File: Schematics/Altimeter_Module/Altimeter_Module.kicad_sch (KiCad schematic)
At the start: 102 parts, among them J1 Stack Male Edge Connector, J2 Main E-Match, J3 Drogue E-Match, J4 USB_B_Micro, J5 SWD_01x04_Pin, Q1 AO3400A, Q2 AO4406AL, Q3 AO3400A, Q4 AO3400A, Q5 AO4406AL, SW1 SW_STM_RESET, SW2 SW_STM_BOOT_MODE, U1 KX134-1211, U10 ACS70331EOLC, U12 AMS1117-3.3, U2 MS560702BA03-50, U3 W25Q128JVS, U4 LM66100DCKR, U5 LM66100DCKR, U6 STM32F103CBTx, U7 LM66100DCKR, U8 ISO1042BDWVR, U9 MPU-6050, Y1 X322516MMB4SI

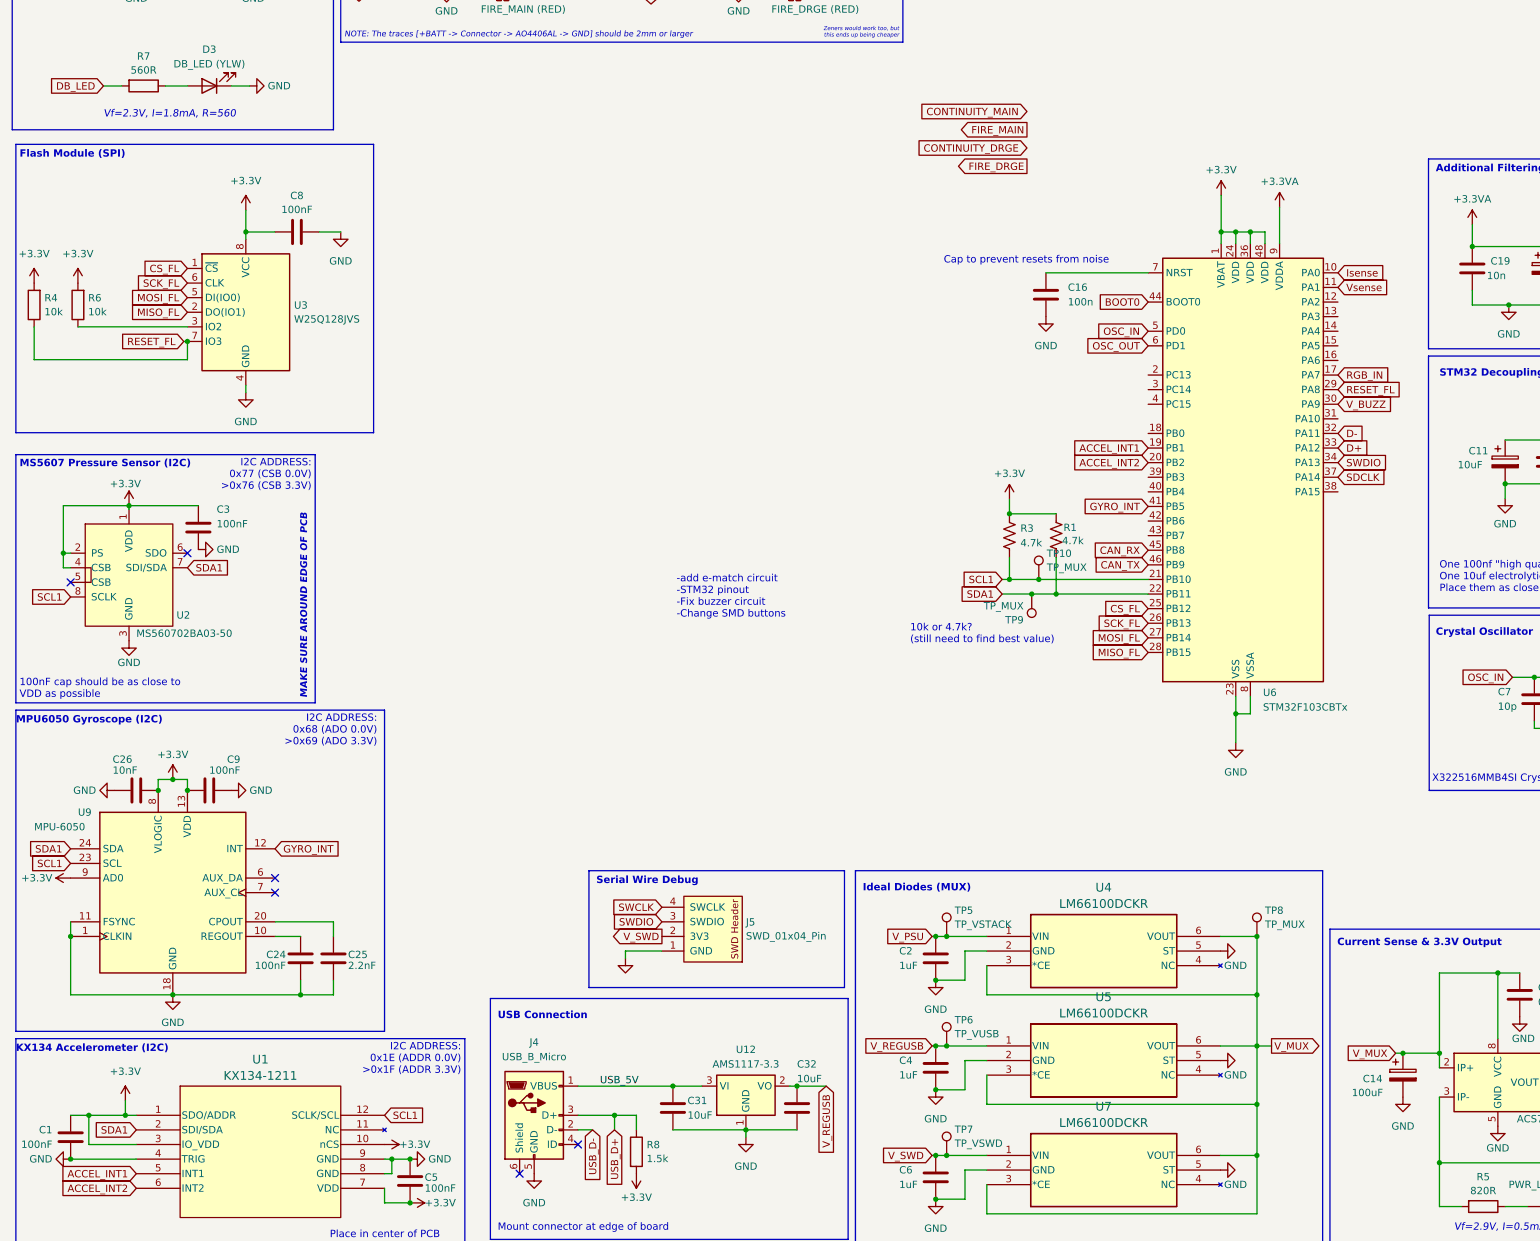
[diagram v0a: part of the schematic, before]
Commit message: Updated STM32 pinout
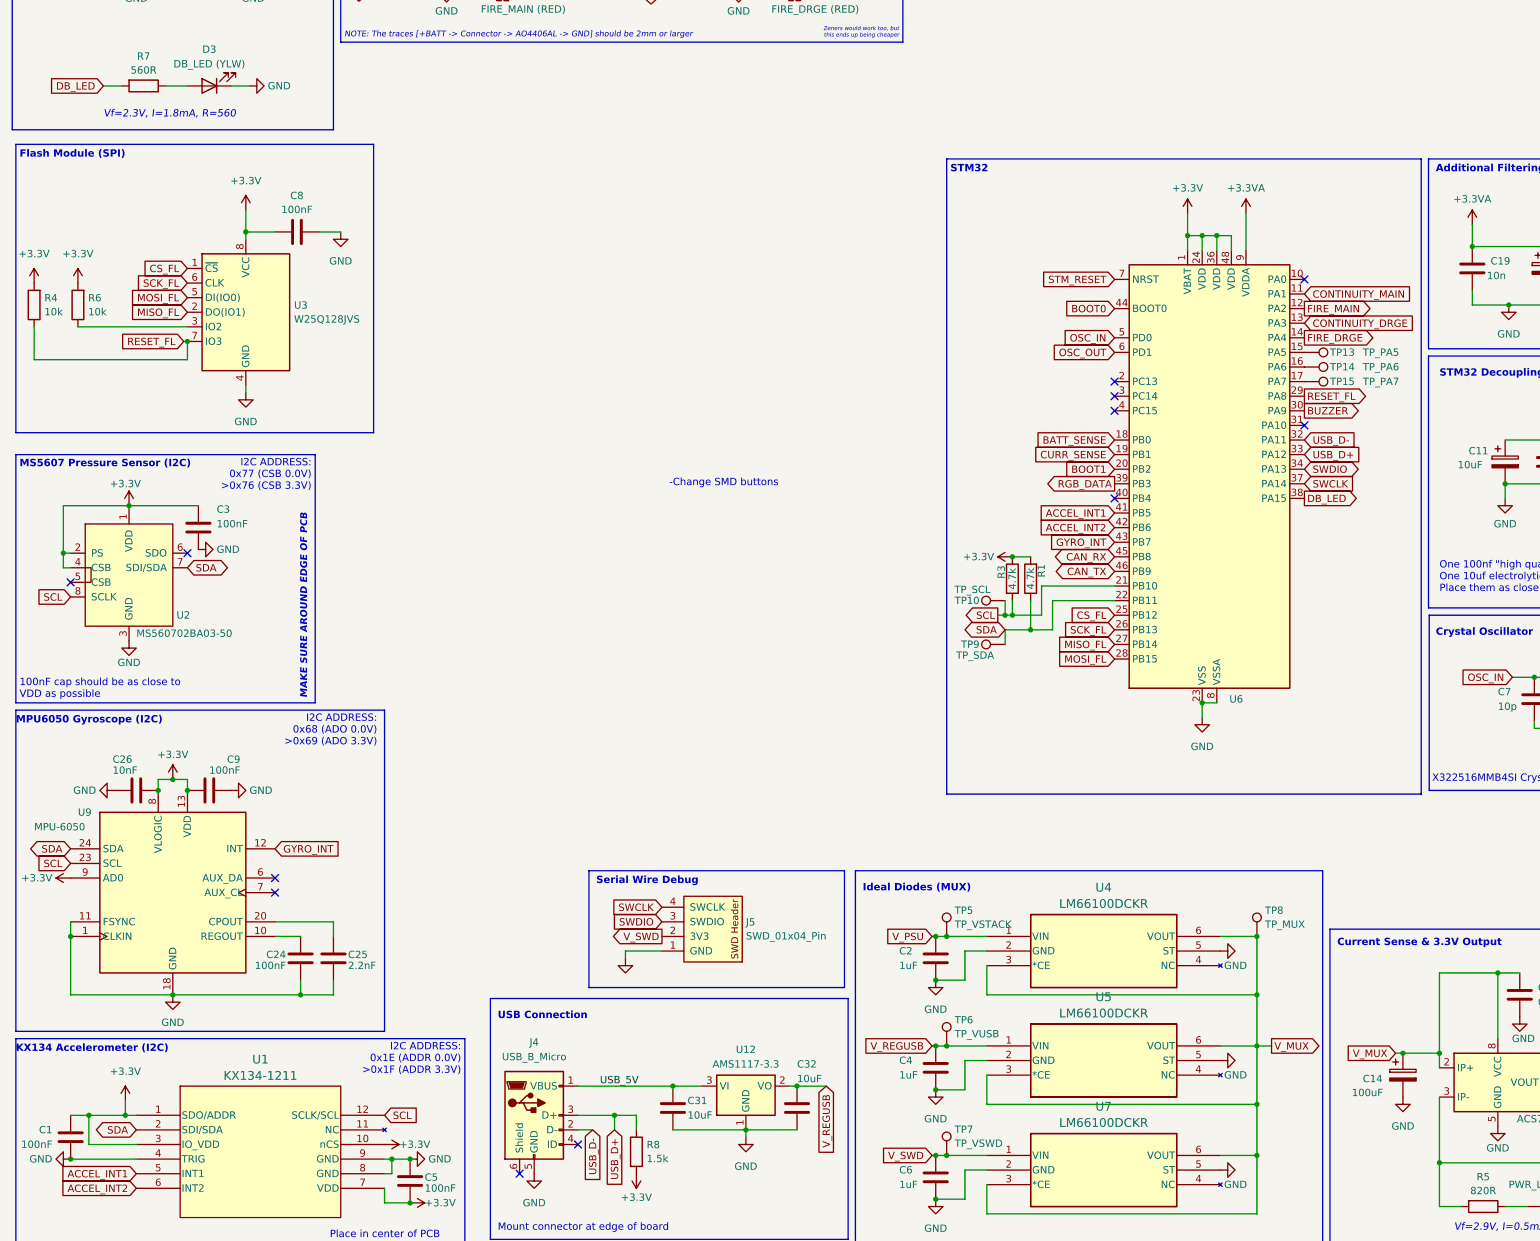
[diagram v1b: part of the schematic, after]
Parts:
- removed C16: 100n, symbol Device:C
- removed R1, R3: 4.7k, symbol Device:R_US
- added R1, R3: 4.7k, Resistor_SMD:R_0603_1608Metric, symbol Device:R
- added TP13: TP_PA5, TestPoint:TestPoint_Pad_1.5x1.5mm, symbol Connector:TestPoint
- added TP14: TP_PA6, TestPoint:TestPoint_Pad_1.5x1.5mm, symbol Connector:TestPoint
- added TP15: TP_PA7, TestPoint:TestPoint_Pad_1.5x1.5mm, symbol Connector:TestPoint
- TP10: value TP_MUX -> TP_SCL
- TP9: value TP_MUX -> TP_SDA
- U6: LCSC (none) -> C8304
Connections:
- net D+ is gone; now on net USB_D+: U6.33 (PA12)
- net D- is gone; now on net USB_D-: U6.32 (PA11)
- net SDCLK is gone; now on net SWCLK: U6.37 (PA14)
- net V_BUZZ is gone; now on net BUZZER: U6.30 (PA9)
- net Vsense is gone; now on net CONTINUITY_MAIN: U6.11 (PA1)
- net +3.3V: now also R1.2, R3.1
- net ACCEL_INT1: now also U6.41 (PB5); no longer U6.19 (PB1)
- net ACCEL_INT2: now also U6.42 (PB6); no longer U6.20 (PB2)
- net BATT_SENSE: now also U6.18 (PB0)
- net BOOT1: now also U6.20 (PB2)
- net CONTINUITY_DRGE: now also U6.13 (PA3)
- net CURR_SENSE: now also U6.19 (PB1)
- net DB_LED: now also U6.38 (PA15)
- net FIRE_DRGE: now also U6.14 (PA4)
- net FIRE_MAIN: now also U6.12 (PA2)
- net GYRO_INT: now also U6.43 (PB7); no longer U6.41 (PB5)
- net MISO_FL: now also U6.27 (PB14); no longer U6.28 (PB15)
- net MOSI_FL: now also U6.28 (PB15); no longer U6.27 (PB14)
- net RGB_DATA: now also U6.39 (PB3)
- net STM_RESET: now also U6.7 (NRST)
- net at U6.15 (PA5): now also TP13.1
- net at U6.16 (PA6): now also TP14.1
- net Isense: no longer names the net of U6.10 (PA0)
- net RGB_IN: no longer names the net of U6.17 (PA7)
- net RGB_IN: now also TP15.1
- net SCL1 renamed SCL
- net SCL: now also R3.2
- net SDA1 renamed SDA
- net SDA: now also R1.1
- no-connect marks 10 -> 16
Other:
- note added: "-Change SMD buttons"
- note added: "STM32"
- note removed: "-add e-match circuit -STM32 pinout -Fix buzzer circuit -Change SMD buttons"
- note removed: "10k or 4.7k? (still need to find best value)"
- note removed: "Cap to prevent resets from noise"
- moved on the sheet: TP10, TP9, U6

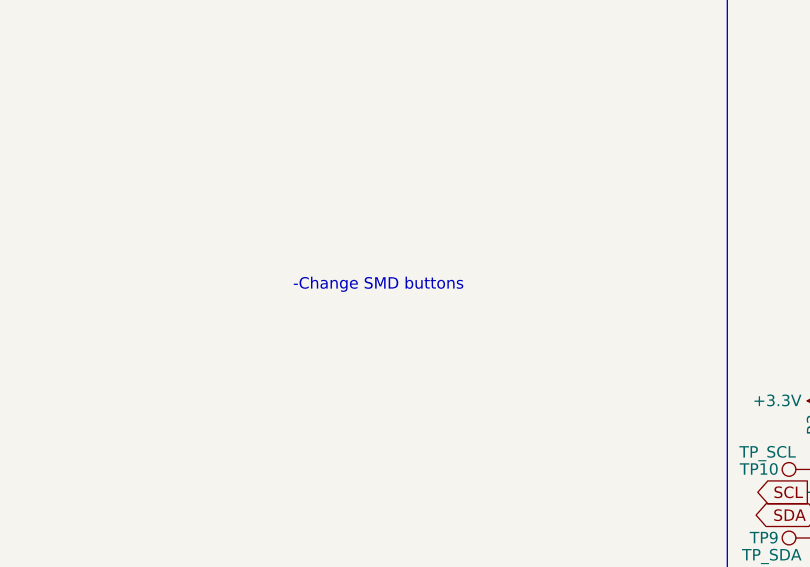
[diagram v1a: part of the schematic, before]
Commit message: Replaced bootmote & reset button footprints
Changed from PTS636SK to a PTS1187A as the latter is a JLCPCB basic component (cost-saving)
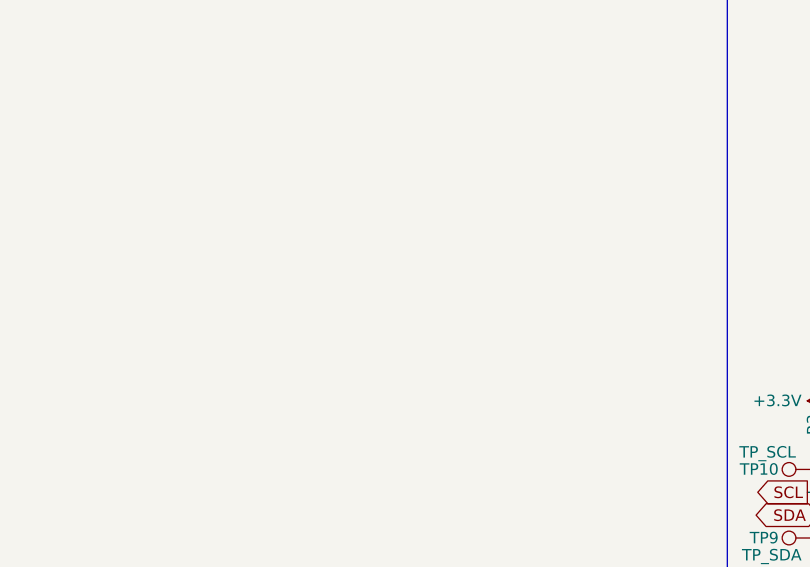
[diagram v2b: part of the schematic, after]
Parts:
- SW1, SW2: footprint PTS636:PTS636_SK43_SMTR_LFS -> Button_Switch_SMD:SW_Push_1P1T_XKB_TS-1187A; Digikey PTS636 SK43 SMTR LFS -> (none); LCSC (none) -> C318884
- U1: footprint LGA12_2X2X0P9_ROM -> Package_LGA:LGA-12_2x2mm_P0.5mm
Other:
- note removed: "-Change SMD buttons"
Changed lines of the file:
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@@
     (effects (font (size 1.27 1.27)) (justify left bottom))
   )
-  (text "-Change SMD buttons" (at 127 134.62 0)
-    (effects (font (size 1.27 1.27)) (justify left bottom))
-  )
   (text "One 100nf \"high quality ceramic\" capacitor for each VDD and VBAT\nOne 10uf electrolytic capacitor for bulk filtering.\nPlace them as close as possible to the IC - one cap per input pin"
     (at 260.985 153.035 0)
@@
       (effects (font (size 1.27 1.27)))
     )
-    (property "Footprint" "PTS636:PTS636_SK43_SMTR_LFS" (at 358.775 130.175 0)
+    (property "Footprint" "Button_Switch_SMD:SW_Push_1P1T_XKB_TS-1187A" (at 358.775 130.175 0)
       (effects (font (size 1.27 1.27)) hide)
     )
-    (property "Datasheet" "https://www.ckswitches.com/media/2779/pts636.pdf" (at 358.775 130.175 0)
+    (property "Datasheet" "https://datasheet.lcsc.com/lcsc/2304140030_XKB-Connection-TS-1187A-B-A-B_C318884.pdf" (at 358.775 130.175 0)
       (effects (font (size 1.27 1.27)) hide)
     )
-    (property "Digikey" "PTS636 SK43 SMTR LFS" (at 358.775 135.255 0)
+    (property "LCSC" "C318884" (at 358.775 135.255 0)
       (effects (font (size 1.27 1.27)) hide)
     )
@@
       (effects (font (size 1.524 1.524)))
     )
-    (property "Footprint" "LGA12_2X2X0P9_ROM" (at 34.29 243.84 0)
+    (property "Footprint" "Package_LGA:LGA-12_2x2mm_P0.5mm" (at 34.29 243.84 0)
       (effects (font (size 1.27 1.27) italic) hide)
     )
-    (property "Datasheet" "KX134-1211" (at 34.29 243.84 0)
+    (property "Datasheet" "https://fscdn.rohm.com/kionix/en/datasheet/kx134-1211-e.pdf" (at 34.29 243.84 0)
       (effects (font (size 1.27 1.27) italic) hide)
     )
@@
     )
   )
-  (symbol (lib_id "Switch:SW_Push") (at 368.935 161.925 0) (unit 1)
-    (in_bom yes) (on_board yes) (dnp no) (fields_autoplaced)
-    (property "Reference" "SW2" (at 368.935 154.8597 0)
-      (effects (font (size 1.27 1.27)))
-    )
-    (property "Value" "SW_STM_BOOT_MODE" (at 368.935 157.2839 0)
-      (effects (font (size 1.27 1.27)))
-    )
-    (property "Footprint" "PTS636:PTS636_SK43_SMTR_LFS" (at 368.935 156.845 0)
-      (effects (font (size 1.27 1.27)) hide)
-    )
-    (property "Datasheet" "https://www.ckswitches.com/media/2779/pts636.pdf" (at 368.935 156.845 0)
-      (effects (font (size 1.27 1.27)) hide)
-    )
-    (property "Digikey" "PTS636 SK43 SMTR LFS" (at 368.935 161.925 0)
-      (effects (font (size 1.27 1.27)) hide)
-    )
-    (pin "1")
-    (pin "2")
-    (instances
-      (project "Altimeter_Module"
-        (path "/29db4100-776d-46b8-a17b-170206e82f23"
-          (reference "SW2") (unit 1)
-        )
-      )
-      (project "Communications_Module"
-        (path "/ace06731-9b48-45c3-868d-c65fed1a8f9b"
-          (reference "SW2") (unit 1)
-        )
-      )
-    )
-  )
   (symbol (lib_id "power:GND") (at 173.355 220.345 0) (unit 1)
     (in_bom yes) (on_board yes) (dnp no) (fields_autoplaced)
@@
         )
       )
+    )
+  )
+  (symbol (lib_id "Switch:SW_Push") (at 368.935 161.925 0) (unit 1)
+    (in_bom yes) (on_board yes) (dnp no) (fields_autoplaced)
+    (property "Reference" "SW2" (at 368.935 154.8597 0)
+      (effects (font (size 1.27 1.27)))
+    )
+    (property "Value" "SW_STM_BOOT_MODE" (at 368.935 157.2839 0)
+      (effects (font (size 1.27 1.27)))
+    )
+    (property "Footprint" "Button_Switch_SMD:SW_Push_1P1T_XKB_TS-1187A" (at 368.935 156.845 0)
+      (effects (font (size 1.27 1.27)) hide)
+    )
+    (property "Datasheet" "https://datasheet.lcsc.com/lcsc/2304140030_XKB-Connection-TS-1187A-B-A-B_C318884.pdf" (at 368.935 156.845 0)
+      (effects (font (size 1.27 1.27)) hide)
+    )
+    (property "LCSC" "C318884" (at 368.935 161.925 0)
+      (effects (font (size 1.27 1.27)) hide)
+    )
+    (pin "1")
+    (pin "2")
+    (instances
+      (project "Altimeter_Module"
+        (path "/29db4100-776d-46b8-a17b-170206e82f23"
+          (reference "SW2") (unit 1)
+        )
+      )
+      (project "Communications_Module"
+        (path "/ace06731-9b48-45c3-868d-c65fed1a8f9b"
+          (reference "SW1") (unit 1)
+        )
+      )

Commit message: Rebase to orgin/main
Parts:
- J2, J3: footprint CONN_2-1445057-2_TYCO -> footprints:CONN_2-1445057-2_TYCO
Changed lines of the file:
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@@
       (effects (font (size 1.524 1.524)) (justify left))
     )
-    (property "Footprint" "CONN_2-1445057-2_TYCO" (at 97.79 17.145 0)
+    (property "Footprint" "footprints:CONN_2-1445057-2_TYCO" (at 97.79 17.145 0)
       (effects (font (size 1.27 1.27) italic) hide)
     )
-    (property "Datasheet" "2-1445057-2" (at 97.79 17.145 0)
+    (property "Datasheet" "https://www.te.com/usa-en/product-2-1445057-2.datasheet.pdf" (at 97.79 17.145 0)
       (effects (font (size 1.27 1.27) italic) hide)
     )
@@
       (effects (font (size 1.524 1.524)) (justify left))
     )
-    (property "Footprint" "CONN_2-1445057-2_TYCO" (at 148.59 17.145 0)
+    (property "Footprint" "footprints:CONN_2-1445057-2_TYCO" (at 148.59 17.145 0)
       (effects (font (size 1.27 1.27) italic) hide)
     )
-    (property "Datasheet" "2-1445057-2" (at 148.59 17.145 0)
+    (property "Datasheet" "https://www.te.com/usa-en/product-2-1445057-2.datasheet.pdf" (at 148.59 17.145 0)
       (effects (font (size 1.27 1.27) italic) hide)
     )
